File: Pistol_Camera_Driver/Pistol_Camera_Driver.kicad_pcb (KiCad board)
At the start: 2 copper layers, 90.5 x 46.1 mm, 109 parts, among them J1 Screw_Terminal_01x02, J10 Bluetooth, J11 Screw_Terminal_01x02, J12 Screw_Terminal_01x02, J13 I2C, J14 Screw_Terminal_01x02, J15 Screw_Terminal_01x02, J16 Screw_Terminal_01x02, J17 Screw_Terminal_01x02, J2 Objective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

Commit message: v0.2 circuit was completed
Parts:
- removed C20, C22: 22u, Capacitor_SMD:C_0603_1608Metric_Pad1.08x0.95mm_HandSolder
- removed C21, C24: 0.1, Capacitor_SMD:C_0603_1608Metric_Pad1.08x0.95mm_HandSolder
- removed D2, D4: CDBA3100-HF, Diode_SMD:D_SMA
- removed R14, R15, R16, R18, R20, R21, R22, R23, R24, R25, R26, R27, R28, R29, R30, R31, R32, R33, R34, R35, R36, R37, R38, R39: 1, Resistor_SMD:R_0603_1608Metric_Pad0.98x0.95mm_HandSolder
- removed U6, U7, U8, U9: ~, Package_SO:PowerIntegrations_SO-8
- added C30: 22u, Capacitor_SMD:C_0603_1608Metric_Pad1.08x0.95mm_HandSolder, F.Cu at (13.7, 53.0)
- added C31: 22u, Capacitor_SMD:C_0603_1608Metric_Pad1.08x0.95mm_HandSolder, F.Cu at (13.7, 55.5)
- added J19: I2C, Connector_JST:JST_XH_B4B-XH-A_1x04_P2.50mm_Vertical, F.Cu at (15.0, 70.2)
- added L7: 4u7, Inductor_SMD:L_Chilisin_BMRx00040412, F.Cu at (14.9, 77.5)
- added R42: 10k, Resistor_SMD:R_0603_1608Metric_Pad0.98x0.95mm_HandSolder, F.Cu at (13.7, 58.0)
- added R43: 10k, Resistor_SMD:R_0603_1608Metric_Pad0.98x0.95mm_HandSolder, F.Cu at (13.7, 60.5)
- added R44: 10k, Resistor_SMD:R_0603_1608Metric_Pad0.98x0.95mm_HandSolder, F.Cu at (13.7, 63.1)
- added R45: 10k, Resistor_SMD:R_0603_1608Metric_Pad0.98x0.95mm_HandSolder, F.Cu at (13.7, 65.6)
- added R46: 1, Resistor_SMD:R_0603_1608Metric_Pad0.98x0.95mm_HandSolder, F.Cu at (18.0, 53.0)
- added R47: 1, Resistor_SMD:R_0603_1608Metric_Pad0.98x0.95mm_HandSolder, F.Cu at (18.0, 55.5)
- added R48: 1, Resistor_SMD:R_0603_1608Metric_Pad0.98x0.95mm_HandSolder, F.Cu at (18.0, 58.0)
- added R49: 1, Resistor_SMD:R_0603_1608Metric_Pad0.98x0.95mm_HandSolder, F.Cu at (18.0, 60.5)
- added R50: R, Resistor_SMD:R_0603_1608Metric_Pad0.98x0.95mm_HandSolder, F.Cu at (18.0, 63.1)
- added R51: R, Resistor_SMD:R_0603_1608Metric_Pad0.98x0.95mm_HandSolder, F.Cu at (18.0, 65.6)
- added R52: 1, Resistor_SMD:R_0603_1608Metric_Pad0.98x0.95mm_HandSolder, F.Cu at (22.4, 53.0)
- added R53: 1, Resistor_SMD:R_0603_1608Metric_Pad0.98x0.95mm_HandSolder, F.Cu at (22.4, 55.5)
- added R54: 1, Resistor_SMD:R_0603_1608Metric_Pad0.98x0.95mm_HandSolder, F.Cu at (22.4, 58.0)
- added R55: 1, Resistor_SMD:R_0603_1608Metric_Pad0.98x0.95mm_HandSolder, F.Cu at (22.4, 60.5)
- added U11: ~, Package_TO_SOT_SMD:SOT-89-5_Handsoldering, F.Cu at (1.34, 54.9)
- added U12: MT3608, Package_TO_SOT_SMD:SOT-23-6, F.Cu at (20.8, 77.0)
- added U13: ~, Package_TO_SOT_SMD:SOT-89-5_Handsoldering, F.Cu at (1.34, 61.0)
- added U14: ~, Package_TO_SOT_SMD:SOT-89-5_Handsoldering, F.Cu at (1.34, 67.1)
- added U15: ~, Package_TO_SOT_SMD:SOT-89-5_Handsoldering, F.Cu at (1.34, 73.2)
- added VD1: CDBA3100-HF, Diode_SMD:D_SOD-123, F.Cu at (8.63, 53.4)
- added VD2: CDBA3100-HF, Diode_SMD:D_SOD-123, F.Cu at (8.63, 56.8)
- added VD3: CDBA3100-HF, Diode_SMD:D_SOD-123, F.Cu at (8.63, 60.1)
- added VD4: CDBA3100-HF, Diode_SMD:D_SOD-123, F.Cu at (8.63, 63.5)
- added VD5: CDBA3100-HF, Diode_SMD:D_SOD-123, F.Cu at (8.63, 66.8)
- added VD6: CDBA3100-HF, Diode_SMD:D_SOD-123, F.Cu at (8.63, 70.2)
- added VD7: CDBA3100-HF, Diode_SMD:D_SOD-123, F.Cu at (8.63, 73.5)
- C13, C15, C16, C17, C19, C3: footprint Capacitor_SMD:C_0603_1608Metric_Pad1.08x0.95mm_HandSolder -> Capacitor_SMD:C_0805_2012Metric_Pad1.18x1.45mm_HandSolder
- C14, C18: value 0.1 -> 22u; footprint Capacitor_SMD:C_0603_1608Metric_Pad1.08x0.95mm_HandSolder -> Capacitor_SMD:C_0805_2012Metric_Pad1.18x1.45mm_HandSolder
- J10: value Bluetooth -> I2C; footprint Connector_PinSocket_2.54mm:PinSocket_1x04_P2.54mm_Vertical -> Connector_JST:JST_XH_B4B-XH-A_1x04_P2.50mm_Vertical
- J13: footprint Connector_PinSocket_2.54mm:PinSocket_1x04_P2.54mm_Vertical -> Connector_JST:JST_XH_B4B-XH-A_1x04_P2.50mm_Vertical
- L1, L2, L3, L4: value 4u7 -> 47uH; footprint Inductor_SMD:L_Chilisin_BMRx00040412 -> Inductor_SMD:L_APV_ANR5045
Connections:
- C13 pad 1: Net-(J7-Pin_1) -> Net-(Je1-Pin_1)
- C13 pad 2: GND -> Net-(Je1-Pin_2)
- C14 pad 2: +5V -> VPP
- C15 pad 1: +5V -> Net-(J7-Pin_1)
- C15 pad 2: GND -> Net-(J7-Pin_2)
- C16 pad 1: +5V -> Net-(J9-Pin_1)
- C16 pad 2: GND -> Net-(J9-Pin_2)
- C17 pad 1: Net-(Je1-Pin_1) -> GND
- C17 pad 2: GND -> VPP
- C18 pad 1: GND -> Net-(J12-Pin_1)
- C18 pad 2: +5V -> Net-(J12-Pin_2)
- C19 pad 1: +5V -> GND
- C19 pad 2: GND -> VPP
- C3 pad 1: Net-(J9-Pin_1) -> GND
- C3 pad 2: GND -> VPP
- J3 pad 1: VPP -> VBUS
- L1 pad 2: Net-(J7-Pin_1) -> Net-(J7-Pin_2)
- L2 pad 2: Net-(Je1-Pin_1) -> Net-(J12-Pin_2)
- L3 pad 2: Net-(J9-Pin_1) -> Net-(J9-Pin_2)
- L4 pad 2: Net-(J12-Pin_1) -> Net-(Je1-Pin_2)

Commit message: v0.3 actual state
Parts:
- removed C23: 470uF, Capacitor_SMD:CP_Elec_10x10.5
- removed C26: 180uF, Capacitor_SMD:CP_Elec_6.3x7.7
- removed Je1: Screw_Terminal_01x02, Connector_PinSocket_2.54mm:PinSocket_1x02_P2.54mm_Vertical
- removed U13, U14, U15: ~, Package_TO_SOT_SMD:SOT-89-5_Handsoldering
- added C20: 470uF, Capacitor_THT:CP_Radial_D8.0mm_P3.50mm, F.Cu at (35.9, 61.2)
- added C21: 330uF, Capacitor_THT:CP_Radial_D8.0mm_P3.50mm, F.Cu at (51.1, 66.5)
- added J18: Screw_Terminal_01x02, Connector_JST:JST_XH_B2B-XH-A_1x02_P2.50mm_Vertical, F.Cu at (88.5, 57.7)
- added R14: 1, Resistor_SMD:R_0603_1608Metric_Pad0.98x0.95mm_HandSolder, F.Cu at (82.1, 45.1)
- added R15: 1, Resistor_SMD:R_0603_1608Metric_Pad0.98x0.95mm_HandSolder, F.Cu at (80.6, 45.1)
- added R16: 1, Resistor_SMD:R_0603_1608Metric_Pad0.98x0.95mm_HandSolder, F.Cu at (79.1, 45.1)
- added R18: 1, Resistor_SMD:R_0603_1608Metric_Pad0.98x0.95mm_HandSolder, F.Cu at (77.6, 45.1)
- added R20: 1, Resistor_SMD:R_0603_1608Metric_Pad0.98x0.95mm_HandSolder, F.Cu at (84.4, 30.3)
- added R21: 1, Resistor_SMD:R_0603_1608Metric_Pad0.98x0.95mm_HandSolder, F.Cu at (85.9, 30.3)
- added R22: 1, Resistor_SMD:R_0603_1608Metric_Pad0.98x0.95mm_HandSolder, F.Cu at (81.3, 30.3)
- added R23: 1, Resistor_SMD:R_0603_1608Metric_Pad0.98x0.95mm_HandSolder, F.Cu at (82.8, 30.3)
- added R24: 1, Resistor_SMD:R_0603_1608Metric_Pad0.98x0.95mm_HandSolder, F.Cu at (78.2, 74.7)
- added R25: 1, Resistor_SMD:R_0603_1608Metric_Pad0.98x0.95mm_HandSolder, F.Cu at (79.8, 74.7)
- added R26: 1, Resistor_SMD:R_0603_1608Metric_Pad0.98x0.95mm_HandSolder, F.Cu at (81.3, 74.7)
- added R27: 1, Resistor_SMD:R_0603_1608Metric_Pad0.98x0.95mm_HandSolder, F.Cu at (82.9, 74.7)
- added R28: 1, Resistor_SMD:R_0603_1608Metric_Pad0.98x0.95mm_HandSolder, F.Cu at (79.7, 60.1)
- added R29: 1, Resistor_SMD:R_0603_1608Metric_Pad0.98x0.95mm_HandSolder, F.Cu at (81.3, 60.1)
- added R30: 1, Resistor_SMD:R_0603_1608Metric_Pad0.98x0.95mm_HandSolder, F.Cu at (82.8, 60.1)
- added R31: 1, Resistor_SMD:R_0603_1608Metric_Pad0.98x0.95mm_HandSolder, F.Cu at (84.3, 60.1)
- added U6: ~, Package_TO_SOT_SMD:SOT-89-5, F.Cu at (78.7, 70.4)
- added U7: ~, Package_TO_SOT_SMD:SOT-89-5, F.Cu at (81.9, 26.0)
- added U8: ~, Package_TO_SOT_SMD:SOT-89-5, F.Cu at (81.0, 40.9)
- C4: footprint Capacitor_SMD:CP_Elec_10x10.5 -> Capacitor_THT:CP_Radial_D8.0mm_P3.50mm
- C6: value 180uF -> 330uF; footprint Capacitor_SMD:CP_Elec_6.3x7.7 -> Capacitor_THT:CP_Radial_D8.0mm_P3.50mm
- J1, J12, J14, J15, J16, J17, J3, J4, J5, J7, J8, J9: footprint Connector_PinSocket_2.54mm:PinSocket_1x02_P2.54mm_Vertical -> Connector_JST:JST_XH_B2B-XH-A_1x02_P2.50mm_Vertical
- J6: footprint Connector_PinSocket_2.54mm:PinSocket_1x05_P2.54mm_Vertical -> Connector_JST:JST_XH_B5B-XH-A_1x05_P2.50mm_Vertical
- U11: footprint Package_TO_SOT_SMD:SOT-89-5_Handsoldering -> Package_TO_SOT_SMD:SOT-89-5
- moved J16 116.5 mm to (161.3, 28.6), turned to 0 degrees
- moved J15 115.9 mm to (161.8, 35.8), turned to 0 degrees
- moved J17 113.0 mm to (161.6, 64.0), turned to 0 degrees
- moved J14 112.5 mm to (161.8, 42.6), turned to 0 degrees
- moved J8 97.6 mm to (161.7, 49.5)
- moved J4 96.3 mm to (140.9, 18.6), turned to 0 degrees
- moved J5 93.0 mm to (161.8, 56.5)
- moved VD7 89.6 mm to (96.7, 57.0), turned to 180 degrees
- moved R44 82.7 mm to (85.8, 22.7), turned to 90 degrees
- moved U11 79.2 mm to (80.5, 55.8), turned to 180 degrees
- moved VD3 77.1 mm to (77.8, 26.0), turned to 90 degrees
- moved R45 76.6 mm to (84.9, 37.5), turned to 90 degrees
- moved VD4 72.0 mm to (76.9, 40.7), turned to 90 degrees
- moved R42 71.2 mm to (84.6, 52.6), turned to 90 degrees
- moved R43 68.6 mm to (82.0, 67.1)
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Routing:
- net +5V: track 193.2 -> 78.9 mm
- net PWM_WHITE: track 23.0 -> 3.54 mm
- net PWM_IR: track 39.3 -> 25.3 mm
- net Net-(J12-Pin_2): track 13.3 -> 0.00 mm
- net Net-(J18-Pin_2): track 13.2 -> 0.00 mm
- net Net-(J7-Pin_2): track 13.2 -> 0.00 mm
- net GND: track 17.7 -> 29.8 mm
- net Net-(J9-Pin_2): track 12.0 -> 0.00 mm
- net PWM_UV: track 31.8 -> 21.7 mm
- net Net-(J12-Pin_1): track 6.21 -> 0.00 mm
- net Net-(J18-Pin_1): track 6.20 -> 0.00 mm
- net Net-(J7-Pin_1): track 6.08 -> 0.00 mm
- net Net-(J9-Pin_1): track 5.81 -> 0.00 mm
- net PWM_RED: track 27.7 -> 22.6 mm
- net SCL: track 7.70 -> 3.19 mm
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
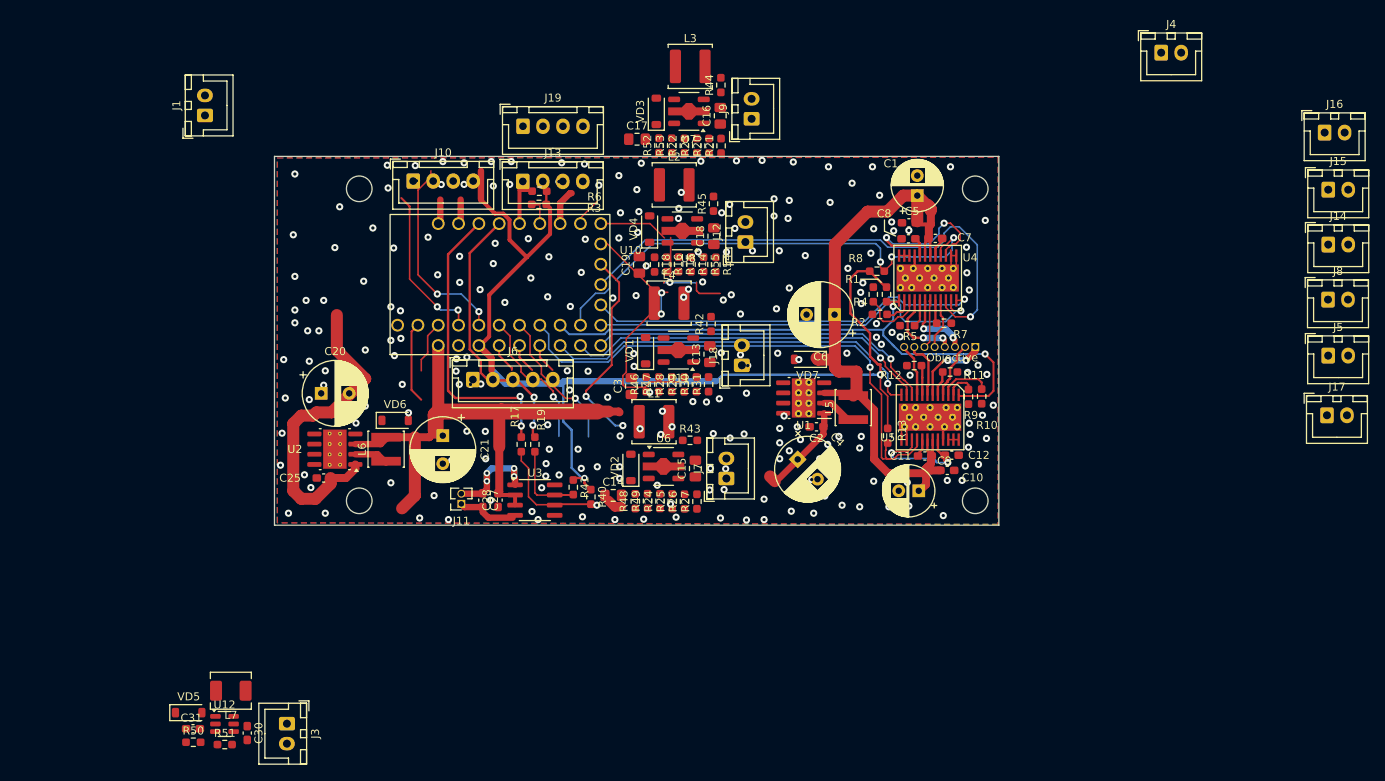
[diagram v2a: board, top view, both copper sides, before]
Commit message: v0.4 draft decomposition completed
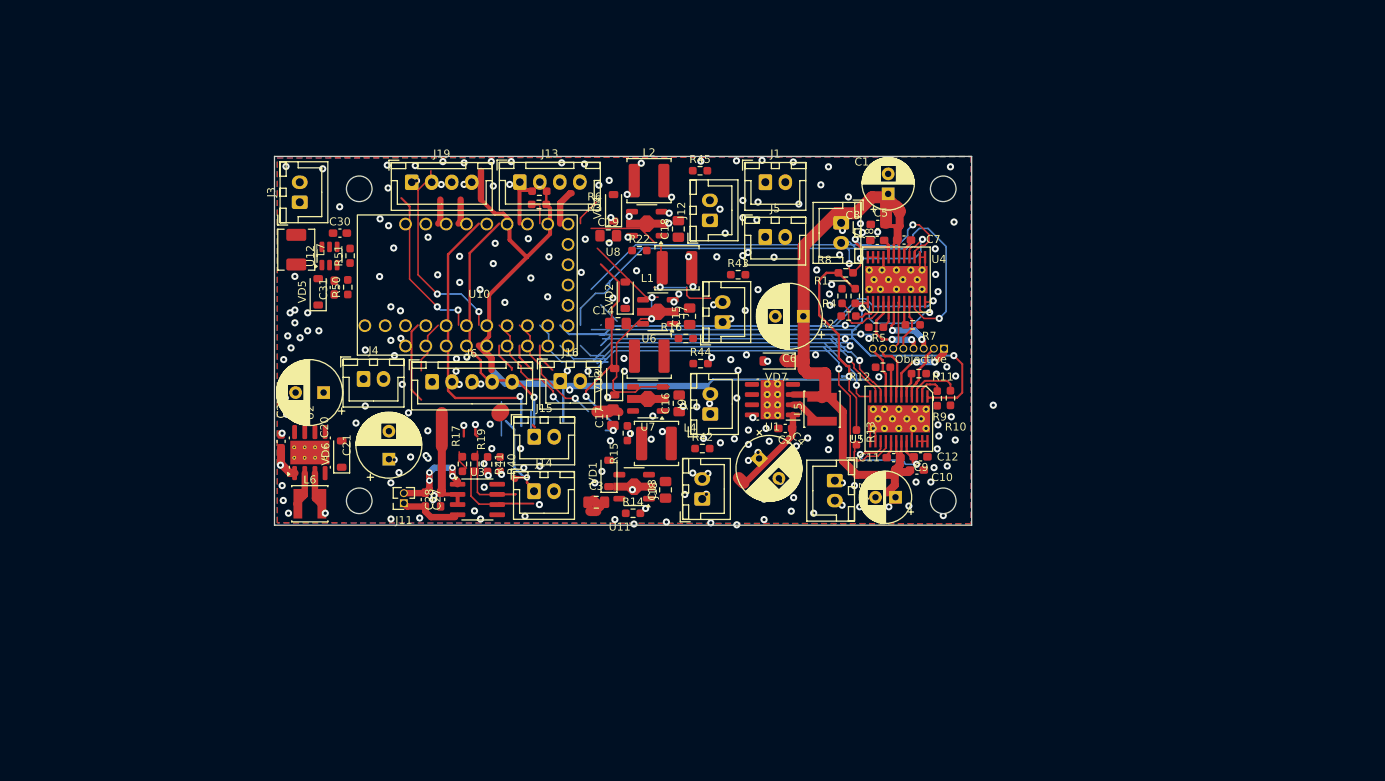
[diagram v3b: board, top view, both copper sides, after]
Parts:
- removed J10: I2C, Connector_JST:JST_XH_B4B-XH-A_1x04_P2.50mm_Vertical
- removed R18, R20, R21, R23, R24, R25, R26, R27, R28, R29, R30, R31, R46, R47, R48, R49, R52, R53, R54, R55: 1, Resistor_SMD:R_0603_1608Metric_Pad0.98x0.95mm_HandSolder
- moved J4 107.7 mm to (41.2, 59.4)
- moved J14 104.0 mm to (62.5, 73.5)
- moved J15 104.0 mm to (62.5, 66.6)
- moved J16 100.5 mm to (65.8, 59.7)
- moved J5 71.9 mm to (91.4, 41.7)
- moved J1 70.5 mm to (91.4, 34.8), turned to 0 degrees
- moved J3 65.2 mm to (33.2, 37.3), turned to 90 degrees
- moved C30 63.6 mm to (38.2, 41.2), turned to 0 degrees
- moved R51 63.1 mm to (39.5, 44.0), turned to 90 degrees
- moved J17 62.1 mm to (100.1, 72.1), turned to -90 degrees
- moved J8 61.6 mm to (100.9, 39.9), turned to -90 degrees
- moved R50 60.1 mm to (39.2, 48.0), turned to 90 degrees
- moved U12 60.0 mm to (36.9, 44.0), turned to 90 degrees
- moved C31 57.9 mm to (37.5, 48.0), turned to 90 degrees
- moved L7 55.7 mm to (32.8, 43.3), turned to -90 degrees
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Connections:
- R14 pad 2: Net-(J12-Pin_1) -> Net-(J18-Pin_1)
- R15 pad 2: Net-(J12-Pin_1) -> Net-(J9-Pin_1)
- R16 pad 2: Net-(J12-Pin_1) -> Net-(J7-Pin_1)
- R22 pad 2: Net-(J9-Pin_1) -> Net-(J12-Pin_1)
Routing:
- net Net-(J7-Pin_1): track 0.00 -> 64.0 mm
- net +3V3: track 133.6 -> 82.9 mm, vias 2 -> 1
- net +5V: track 78.9 -> 39.0 mm
- net Net-(J9-Pin_2): track 0.00 -> 39.0 mm
- net STEP1: track 51.2 -> 18.1 mm
- net DIR1: track 49.3 -> 18.3 mm
- net PWM_IR: track 25.3 -> 0.00 mm, vias 2 -> 0
- net K4: track 20.2 -> 0.00 mm, vias 2 -> 0
- net PWM_RED: track 22.6 -> 4.66 mm, vias 2 -> 0
- net RX: track 3.11 -> 20.2 mm, vias 0 -> 2
- net K3: track 24.9 -> 36.7 mm, vias 2 -> 3
- net K6: track 10.2 -> 0.00 mm
- net PWM_UV: track 21.7 -> 31.8 mm
- net Net-(U6-SW): track 0.00 -> 9.62 mm, vias 0 -> 1
- net VPP: track 39.9 -> 31.6 mm, vias 0 -> 1
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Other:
- board size 90.5 x 46.1 mm -> 87.2 x 46.1 mm

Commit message: v0.5 actual state
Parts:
- R3, R6: moved to B.Cu
- moved R6 8.04 mm to (55.4, 38.0)
- moved R3 5.92 mm to (57.3, 36.5), turned to 0 degrees
- moved C25 4.52 mm to (31.0, 71.7), turned to -90 degrees
- moved R17 3.30 mm to (56.8, 70.0)
- moved R19 3.29 mm to (58.4, 70.0)
- moved R40 2.89 mm to (55.4, 70.0)
- moved R41 2.89 mm to (53.8, 70.0)
- moved VD4 0.11 mm to (72.5, 38.1)
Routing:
- net Solenoid_ON: track 40.2 -> 0.00 mm, vias 2 -> 0
- net Solenoid_DIR: track 37.3 -> 0.00 mm, vias 2 -> 0
- net VPP: track 31.6 -> 64.7 mm
- net +5V: track 39.0 -> 67.2 mm
- net K3: track 36.7 -> 8.64 mm, vias 3 -> 1
- net SDA: track 5.80 -> 26.9 mm, vias 0 -> 1
- net RX: track 20.2 -> 0.00 mm, vias 2 -> 0
- net SCL: track 3.19 -> 23.2 mm
- net PWM_UV: track 31.8 -> 13.4 mm, vias 2 -> 0
- net K2: track 17.9 -> 0.00 mm, vias 1 -> 0
- net GND: track 35.9 -> 20.6 mm
- net K1: track 18.2 -> 3.54 mm
- net VBUS: track 0.00 -> 13.6 mm
- net Net-(J12-Pin_2): track 0.00 -> 10.7 mm
- net Net-(U6-SW): track 9.62 -> 0.00 mm, vias 1 -> 0
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
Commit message: v0.6 actual state
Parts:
- moved R43 3.14 mm to (85.6, 44.4)
- moved R4 2.39 mm to (99.5, 50.9)
- moved R2 2.32 mm to (100.4, 53.4)
- moved R1 2.31 mm to (101.1, 50.8)
- moved R8 1.89 mm to (101.5, 48.0)
- moved C17 1.58 mm to (71.4, 65.5)
- moved J7 1.19 mm to (86.1, 51.1)
- moved VD1 1.03 mm to (70.8, 71.2)
- moved R22 0.99 mm to (74.7, 43.4)
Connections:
- R42 pad 1: PWM_WHITE -> PWM_IR
- R45 pad 1: PWM_IR -> PWM_WHITE
- U11 pad 3: PWM_WHITE -> PWM_IR
- U8 pad 3: PWM_IR -> PWM_WHITE
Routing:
- net VPP: track 64.7 -> 147.8 mm, vias 1 -> 4
- net Net-(J7-Pin_1): track 64.0 -> 8.81 mm
- net K1: track 3.54 -> 52.9 mm
- net PWM_IR: track 0.00 -> 46.3 mm, vias 0 -> 5
- net Strobe Input: track 0.00 -> 34.5 mm
- net STEP1: track 18.1 -> 51.7 mm
- net DIR1: track 18.3 -> 50.9 mm
- net PWM_WHITE: track 0.00 -> 30.3 mm, vias 0 -> 2
- net Net-(J9-Pin_2): track 39.0 -> 9.60 mm
- net PWM_RED: track 0.00 -> 28.2 mm, vias 0 -> 3
- net K4: track 0.00 -> 26.3 mm, vias 0 -> 1
- net K5: track 0.00 -> 25.8 mm
- net PWM_UV: track 13.4 -> 33.4 mm, vias 0 -> 3
- net K3: track 8.64 -> 25.1 mm
- net Net-(J9-Pin_1): track 0.00 -> 11.3 mm
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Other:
- board size 87.2 x 46.1 mm -> 86.6 x 46.1 mm

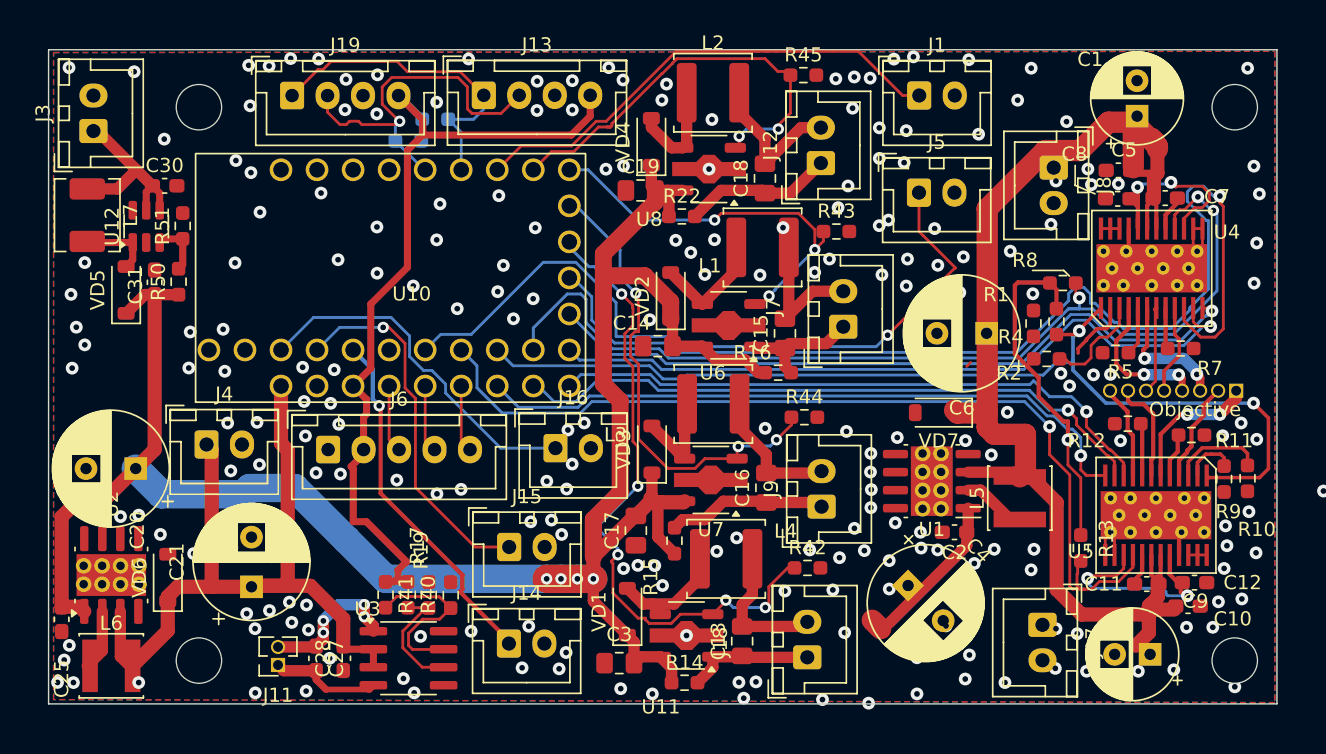
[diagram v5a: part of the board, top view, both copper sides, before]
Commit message: v0.7 draft routung completed
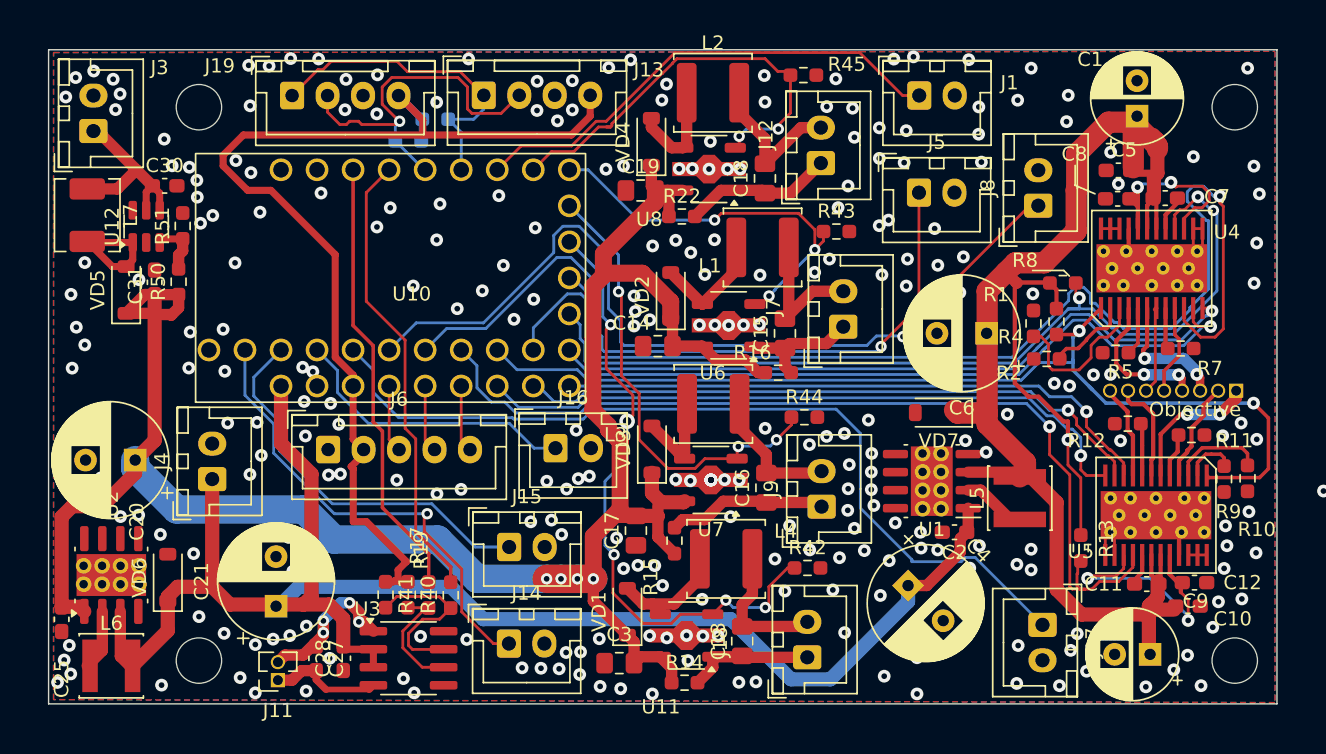
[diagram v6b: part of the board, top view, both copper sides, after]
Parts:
- moved J8 2.89 mm to (99.8, 42.6), turned to 90 degrees
- moved J4 2.47 mm to (41.6, 61.9), turned to 90 degrees
- moved C21 2.21 mm to (46.1, 70.8)
- moved J11 1.07 mm to (46.2, 76.0)
- moved C20 0.60 mm to (36.2, 60.5)
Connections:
- J14 pad 1: K3 -> K6
- J15 pad 1: K4 -> K5
- J16 pad 1: K5 -> K4
- J17 pad 1: K6 -> K3
- R1 pad 1: +3V3 -> +3.3VP
- R13 pad 1: +3V3 -> +3.3VP
- R8 pad 1: +3V3 -> +3.3VP
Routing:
- net K2: track 0.00 -> 61.5 mm, vias 0 -> 1
- net +5V: track 67.2 -> 112.6 mm
- net K3: track 25.1 -> 61.5 mm, vias 1 -> 0
- net K6: track 0.00 -> 33.0 mm, vias 0 -> 1
- net Solenoid_DIR: track 0.00 -> 32.2 mm
- net Solenoid_ON: track 0.00 -> 31.3 mm
- net +3.3VP: track 89.6 -> 117.0 mm, vias 0 -> 1
- net +3V3: track 86.7 -> 75.4 mm, vias 1 -> 0
- net K4: track 26.3 -> 20.6 mm, vias 1 -> 0
- net VPP: track 147.8 -> 153.1 mm
- net Net-(U4-ADECAY): track 6.88 -> 11.0 mm
- net Net-(U12-SW): track 5.13 -> 8.60 mm
- net Net-(U5-CONFIG): track 15.3 -> 17.6 mm
- net K5: track 25.8 -> 27.7 mm
- net DIR1: track 50.9 -> 52.5 mm
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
